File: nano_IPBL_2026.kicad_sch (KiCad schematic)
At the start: 22 parts, among them J3 DB301V-5.0-2P, M1 Motor_Servo, M10 Motor_Servo, M11 Motor_Servo, M12 Motor_Servo, M2 Motor_Servo, M3 Motor_Servo, M4 Motor_Servo, M5 Motor_Servo, M6 Motor_Servo, M7 Motor_Servo, M8 Motor_Servo, M9 Motor_Servo, SW1 SW_DPDT_x2, U1 LM1085-5.0, U2 LM1085-5.0

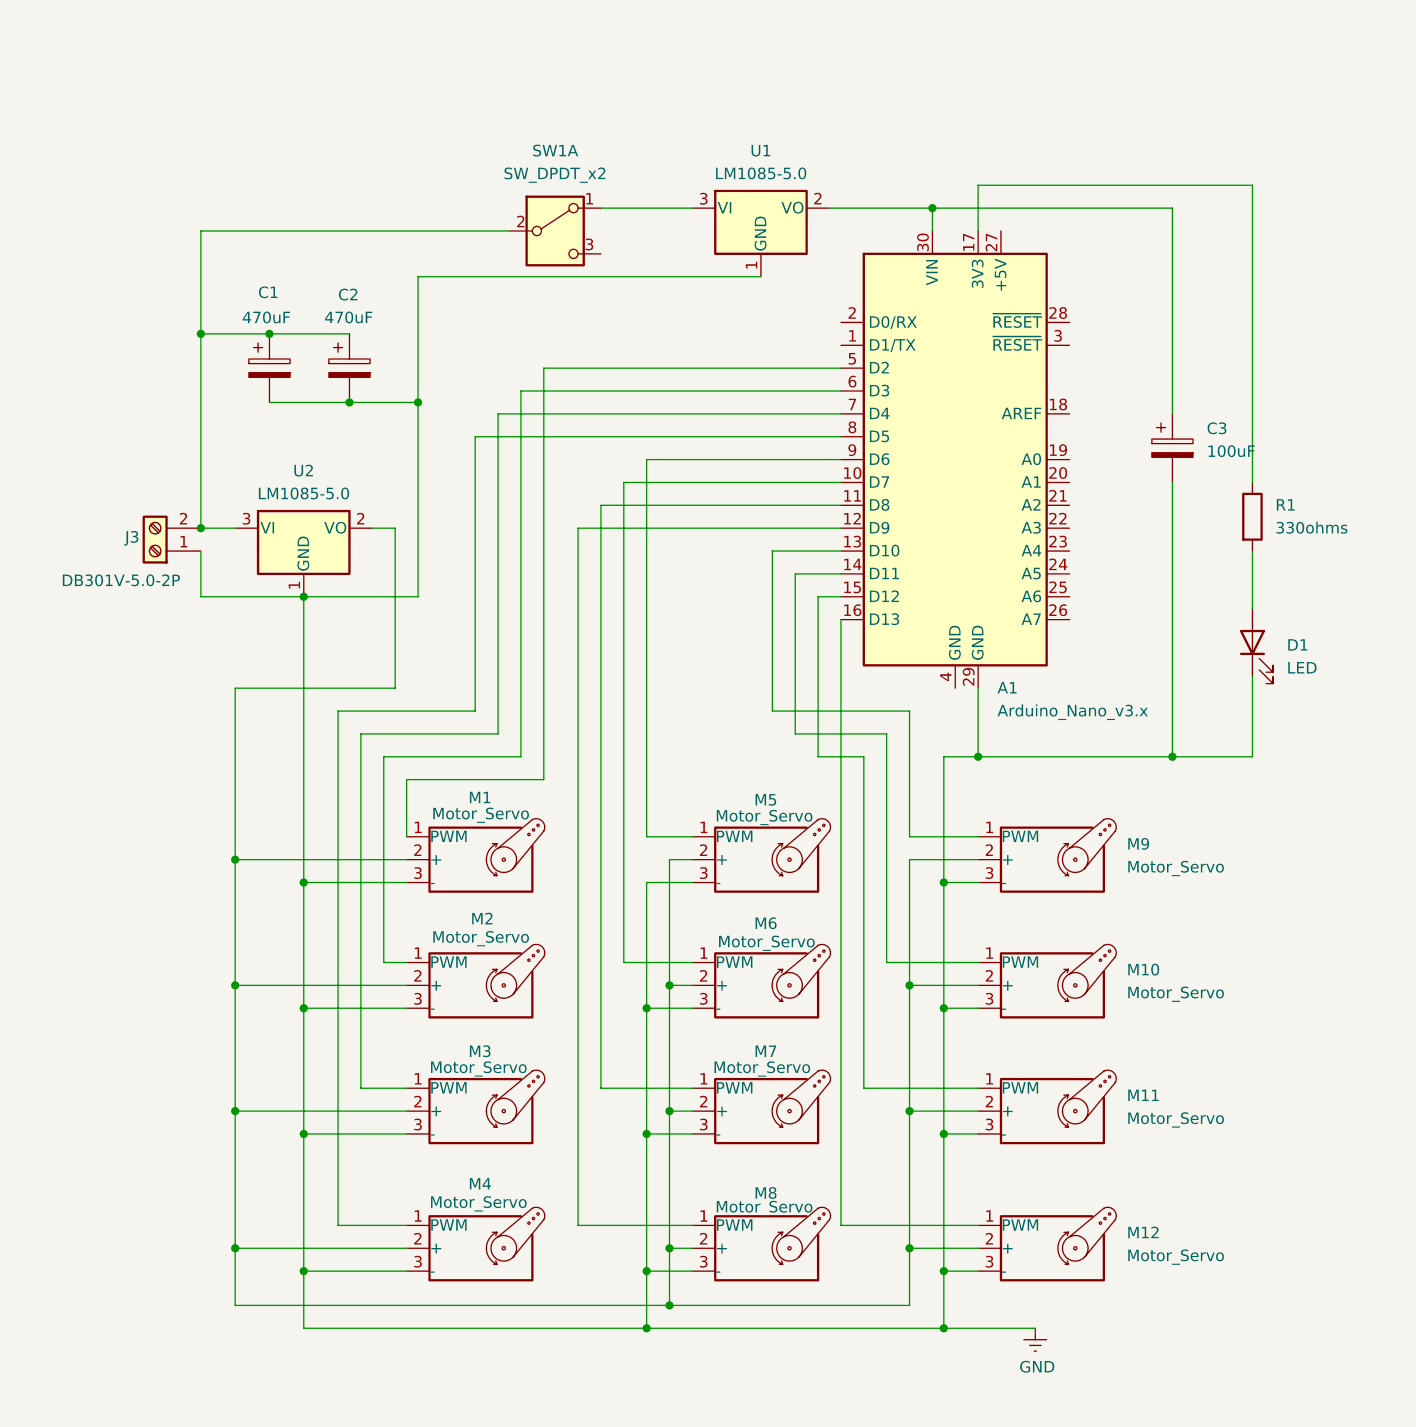
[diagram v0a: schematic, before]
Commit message: Changed padding drill sizes and exported copper layer as SVG
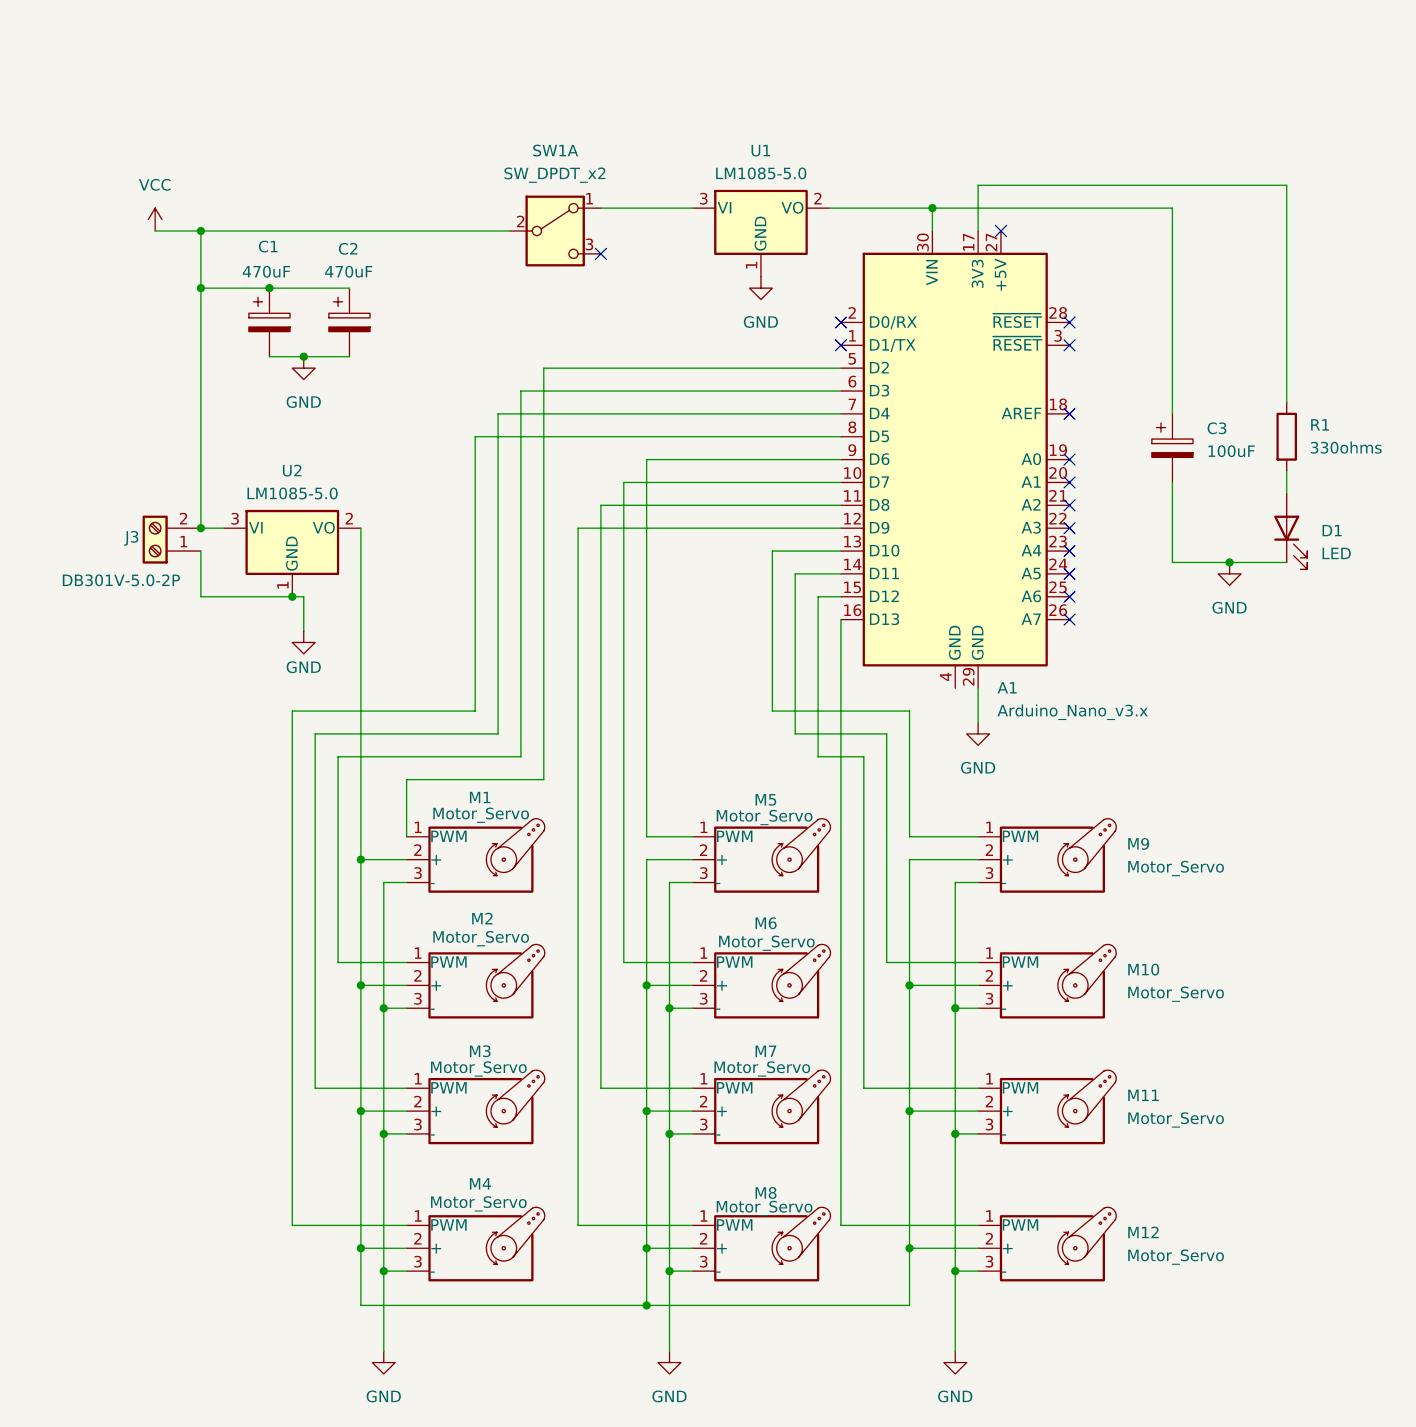
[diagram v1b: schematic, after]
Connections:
- net VCC: now reaches C1.1, C2.1, J3.2 (Pin_2), SW1.2 (B), U2.3 (VI)
- no-connect marks 0 -> 15
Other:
- moved on the sheet: C1, C2, D1, R1, U2

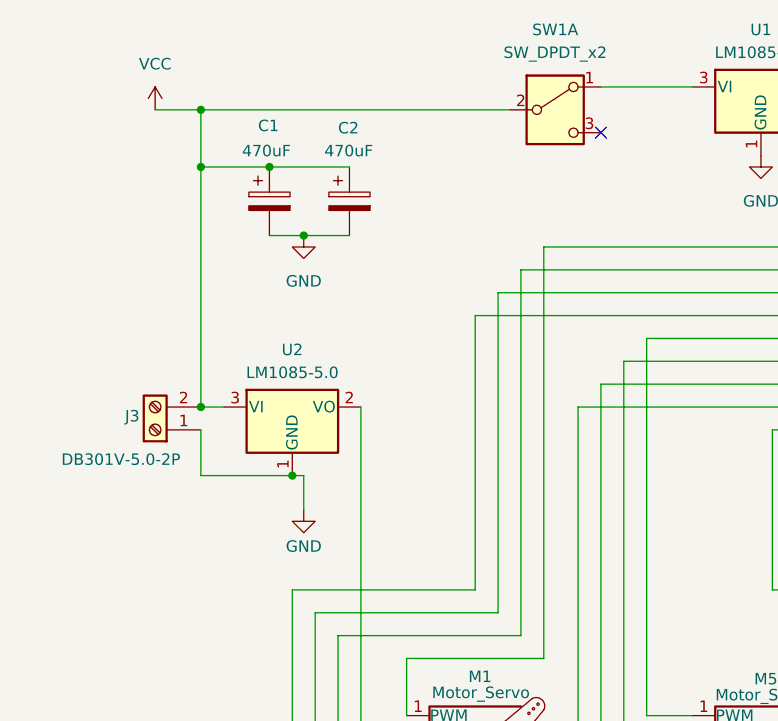
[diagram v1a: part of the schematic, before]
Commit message: Refine PCB design and power circuit
- Fix switch connection to come before voltage regulator (stepdown)
- Increase via diameter to 1mm for better current distribution
- Add 0.25mm copper pad diameter with 0.4mm drill holes
- Rearrange component placement for improved PCB layout
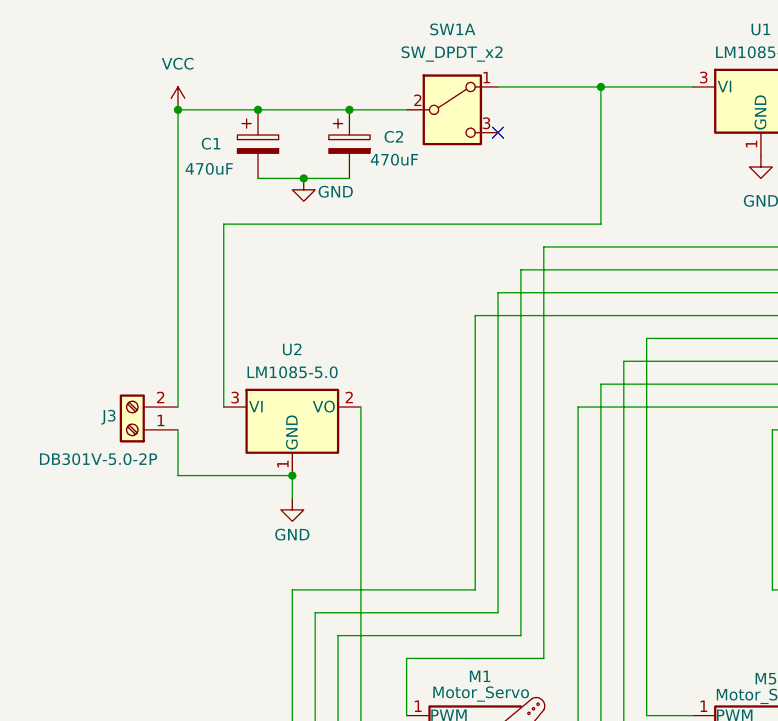
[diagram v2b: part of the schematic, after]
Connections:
- net VCC: no longer U2.3 (VI)
- net at SW1.1 (A), U1.3 (VI): now also U2.3 (VI)
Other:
- moved on the sheet: C1, C2, J3, SW1A

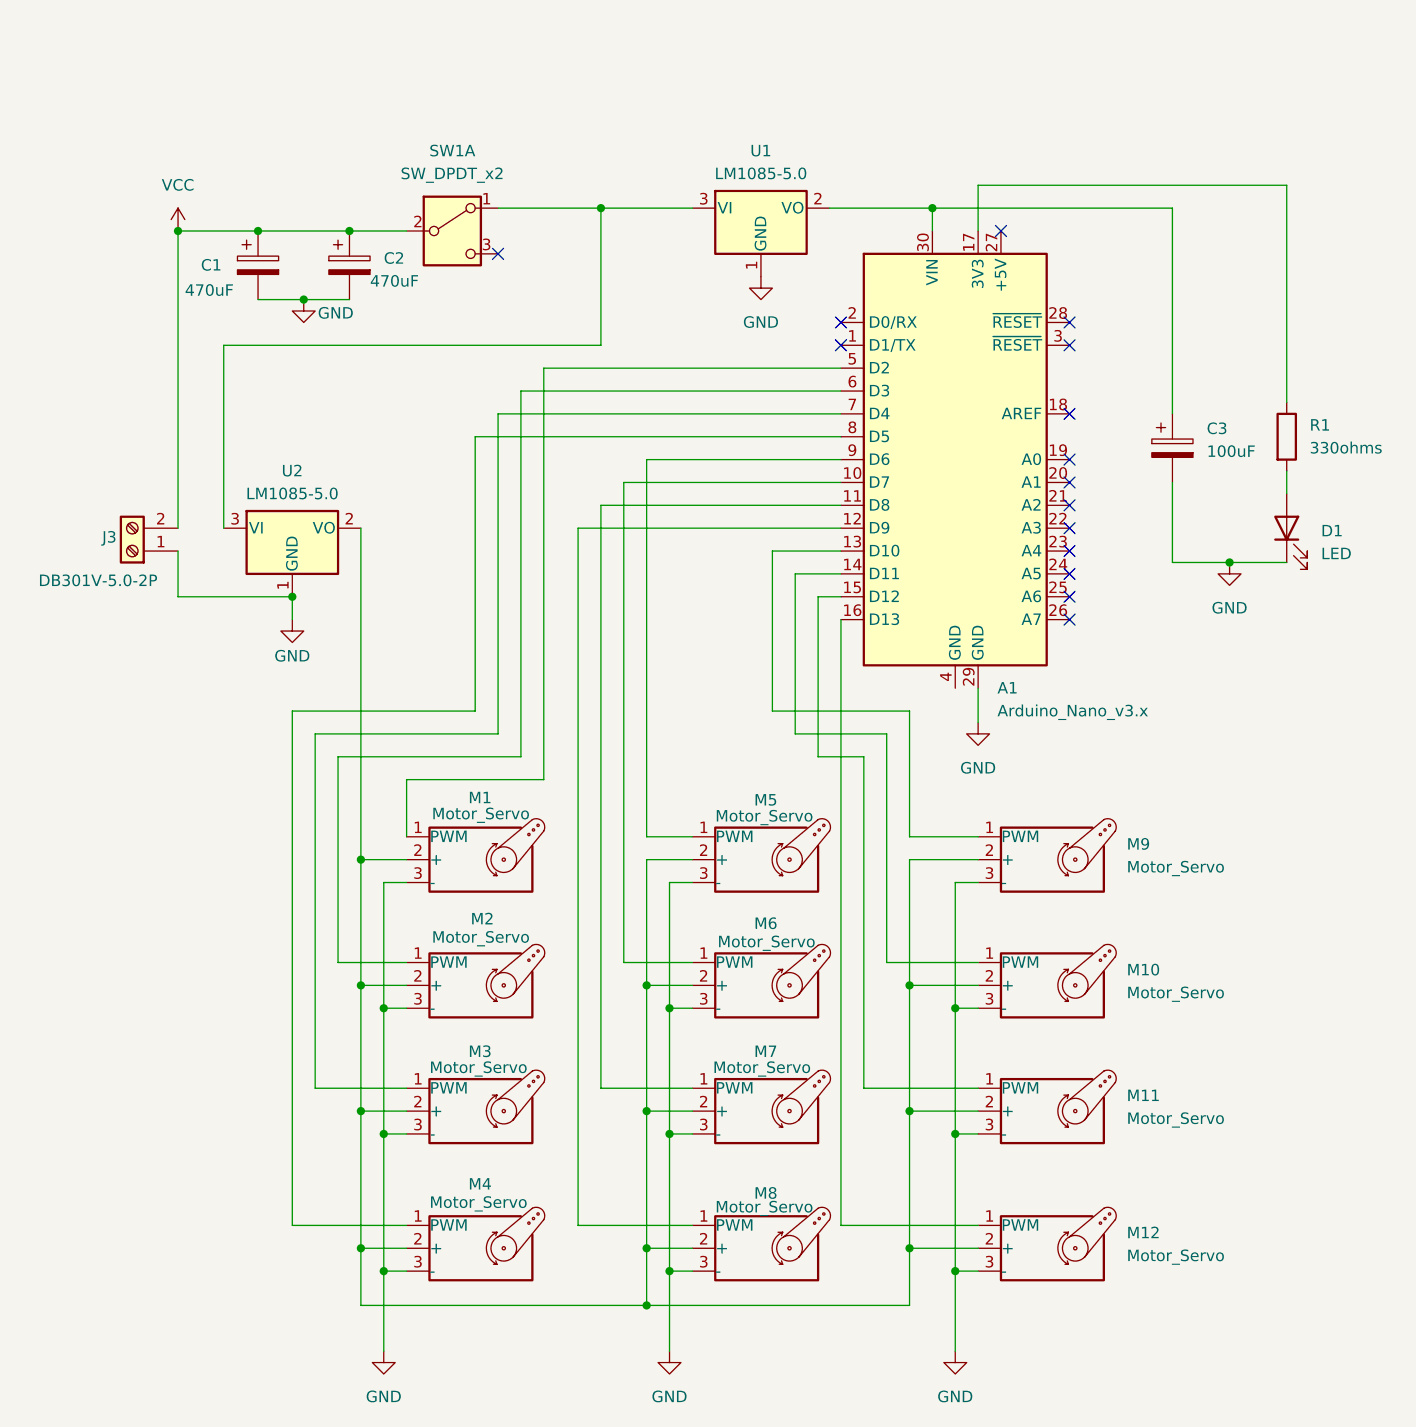
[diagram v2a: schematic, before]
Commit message: Remove step-down regulator and switch, add RX/TX mounting pads
Replace the switch with a mounting pad, remove the step-down regulator,
and add mounting pad connections for RX/TX. Reposition components to
fit the actual enclosure, and move the 100uF capacitor closer to the Nano.
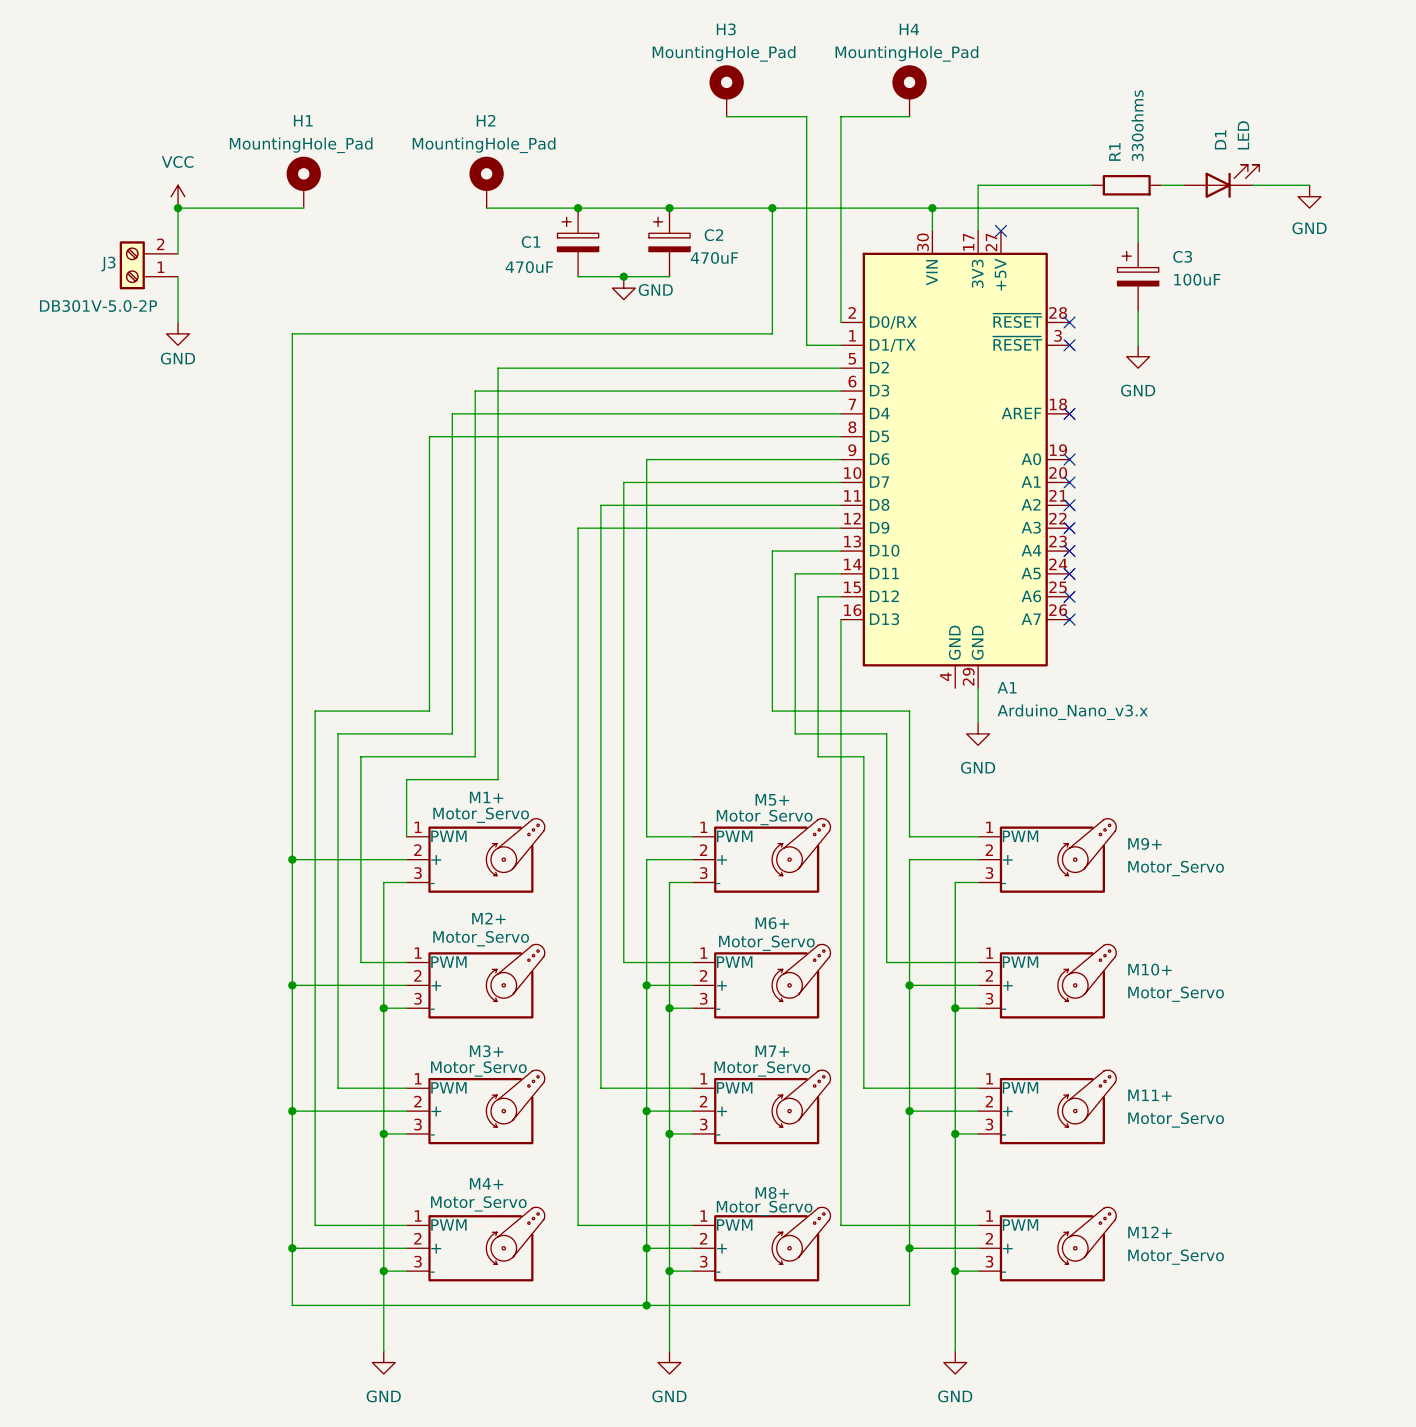
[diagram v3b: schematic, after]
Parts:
- removed SW1: SW_DPDT_x2, lcsc:SW-TH_6P-L5.8-W5.8-P2.00-LS4.5-BL_1, symbol Switch:SW_DPDT_x2
- removed U1, U2: LM1085-5.0, Package_TO_SOT_THT:TO-220-3_Vertical, symbol Regulator_Linear:LM1085-5.0
- added H1, H2, H3, H4: MountingHole_Pad, Arduino_MountingHole:MountingHole_1.2mm_M2_Pad_EDITED, symbol Mechanical:MountingHole_Pad
- renumbered M1 to M1+, M10 to M10+, M11 to M11+, M12 to M12+, M2 to M2+, M3 to M3+, M4 to M4+, M5 to M5+, M6 to M6+, M7 to M7+, M8 to M8+, M9 to M9+
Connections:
- net VCC: now also H1.1; no longer C1.1, C2.1
- net at M1+.2 (+), M10+.2 (+), M11+.2 (+)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: now also A1.30 (VIN), C1.1, C2.1, C3.1, H2.1
- net at A1.1 (D1/TX): now also H3.1
- net at A1.2 (D0/RX): now also H4.1
- no-connect marks 15 -> 12
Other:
- moved on the sheet: C1, C2, C3, D1, J3, R1
